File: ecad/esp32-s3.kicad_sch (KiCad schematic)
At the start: 1 part, among them U4 ESP32-S3

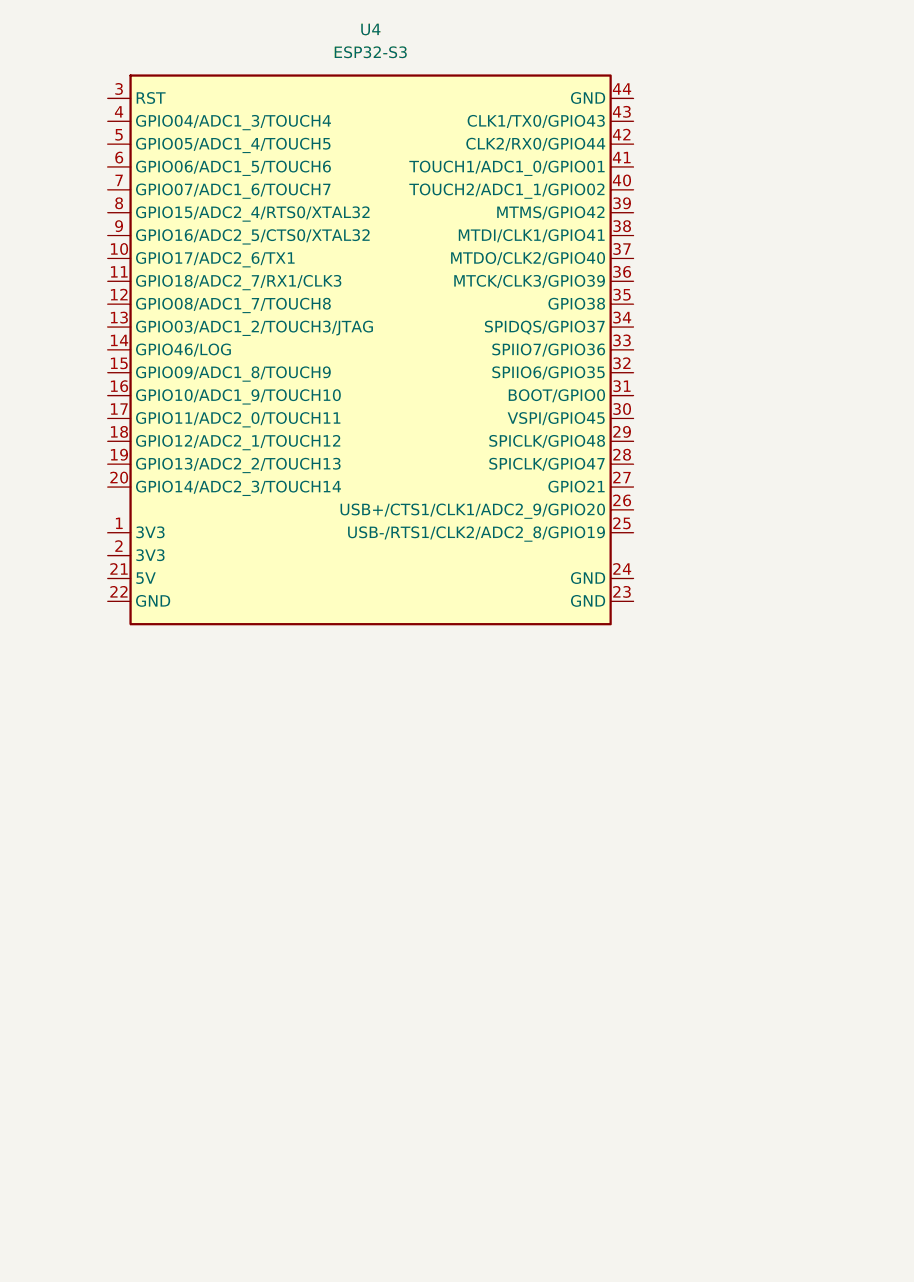
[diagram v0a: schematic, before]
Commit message: fead (ecad): update ESP32-S3 Schematic
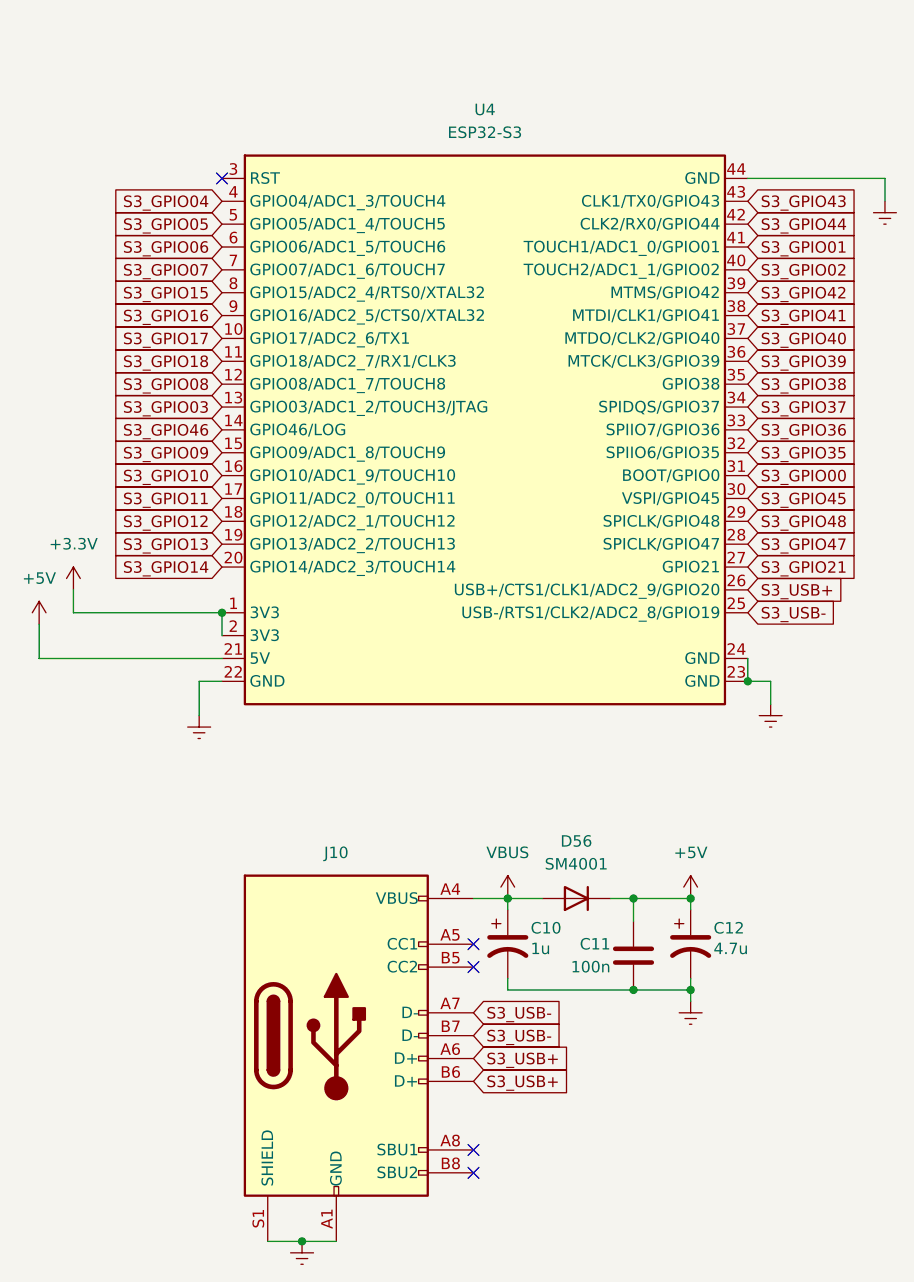
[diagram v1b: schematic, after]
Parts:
- added C10: 1u, Capacitor_SMD:CP_Elec_4x5.4, symbol Device:C_Polarized_US
- added C11: 100n, Capacitor_SMD:C_0805_2012Metric_Pad1.18x1.45mm_HandSolder, symbol Device:C
- added C12: 4.7u, Capacitor_SMD:CP_Elec_4x5.4, symbol Device:C_Polarized_US
- added D56: SM4001, Diode_SMD:D_MELF, symbol Diode:SM4001
- added J10: USB_C, Connector_USB:USB_C_Receptacle_Palconn_UTC16-G, symbol Connector:USB_C_Receptacle_USB2.0_16P
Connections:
- net +3.3V: now reaches U4.1 (3V3)
- net +3.3V: now also U4.2 (3V3)
- net S3_GPIO17: now reaches U4.10 (GPIO17/ADC2_6/TX1)
- net S3_GPIO18: now reaches U4.11 (GPIO18/ADC2_7/RX1/CLK3)
- net S3_GPIO08: now reaches U4.12 (GPIO08/ADC1_7/TOUCH8)
- net S3_GPIO03: now reaches U4.13 (GPIO03/ADC1_2/TOUCH3/JTAG)
- net S3_GPIO46: now reaches U4.14 (GPIO46/LOG)
- net S3_GPIO09: now reaches U4.15 (GPIO09/ADC1_8/TOUCH9)
- net S3_GPIO10: now reaches U4.16 (GPIO10/ADC1_9/TOUCH10)
- net S3_GPIO11: now reaches U4.17 (GPIO11/ADC2_0/TOUCH11)
- net S3_GPIO12: now reaches U4.18 (GPIO12/ADC2_1/TOUCH12)
- net S3_GPIO13: now reaches U4.19 (GPIO13/ADC2_2/TOUCH13)
- net S3_GPIO14: now reaches U4.20 (GPIO14/ADC2_3/TOUCH14)
- net +5V: now reaches U4.21 (5V)
- net +5V: now also C11.1, C12.1, D56.1 (K)
- net Earth: now reaches U4.22 (GND)
- net Earth: now also U4.23 (GND), U4.24 (GND), U4.44 (GND), C10.2, C11.2, C12.2, J10.A1 (GND), J10.A12 (GND), J10.B1 (GND), J10.B12 (GND), J10.S1 (SHIELD)
- net S3_USB-: now reaches U4.25 (USB-/RTS1/CLK2/ADC2_8/GPIO19)
- net S3_USB-: now also J10.A7 (D-), J10.B7 (D-)
- net S3_USB+: now reaches U4.26 (USB+/CTS1/CLK1/ADC2_9/GPIO20)
- net S3_USB+: now also J10.A6 (D+), J10.B6 (D+)
- net S3_GPIO21: now reaches U4.27 (GPIO21)
- net S3_GPIO47: now reaches U4.28 (SPICLK/GPIO47)
- net S3_GPIO48: now reaches U4.29 (SPICLK/GPIO48)
- net S3_GPIO45: now reaches U4.30 (VSPI/GPIO45)
- net S3_GPIO00: now reaches U4.31 (BOOT/GPIO0)
- net S3_GPIO35: now reaches U4.32 (SPIIO6/GPIO35)
- net S3_GPIO36: now reaches U4.33 (SPIIO7/GPIO36)
- net S3_GPIO37: now reaches U4.34 (SPIDQS/GPIO37)
- net S3_GPIO38: now reaches U4.35 (GPIO38)
- net S3_GPIO39: now reaches U4.36 (MTCK/CLK3/GPIO39)
- net S3_GPIO40: now reaches U4.37 (MTDO/CLK2/GPIO40)
- net S3_GPIO41: now reaches U4.38 (MTDI/CLK1/GPIO41)
- net S3_GPIO42: now reaches U4.39 (MTMS/GPIO42)
- net S3_GPIO04: now reaches U4.4 (GPIO04/ADC1_3/TOUCH4)
- net S3_GPIO02: now reaches U4.40 (TOUCH2/ADC1_1/GPIO02)
- net S3_GPIO01: now reaches U4.41 (TOUCH1/ADC1_0/GPIO01)
- net S3_GPIO44: now reaches U4.42 (CLK2/RX0/GPIO44)
- net S3_GPIO43: now reaches U4.43 (CLK1/TX0/GPIO43)
- net S3_GPIO05: now reaches U4.5 (GPIO05/ADC1_4/TOUCH5)
- net S3_GPIO06: now reaches U4.6 (GPIO06/ADC1_5/TOUCH6)
- net S3_GPIO07: now reaches U4.7 (GPIO07/ADC1_6/TOUCH7)
- net S3_GPIO15: now reaches U4.8 (GPIO15/ADC2_4/RTS0/XTAL32)
- net S3_GPIO16: now reaches U4.9 (GPIO16/ADC2_5/CTS0/XTAL32)
- new net VBUS: C10.1, D56.2 (A), J10.A4 (VBUS), J10.A9 (VBUS), J10.B4 (VBUS), J10.B9 (VBUS)
- no-connect marks 0 -> 5
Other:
- title: (none) -> ESP32 AK Shield Schematik drawing S3
- moved on the sheet: U4

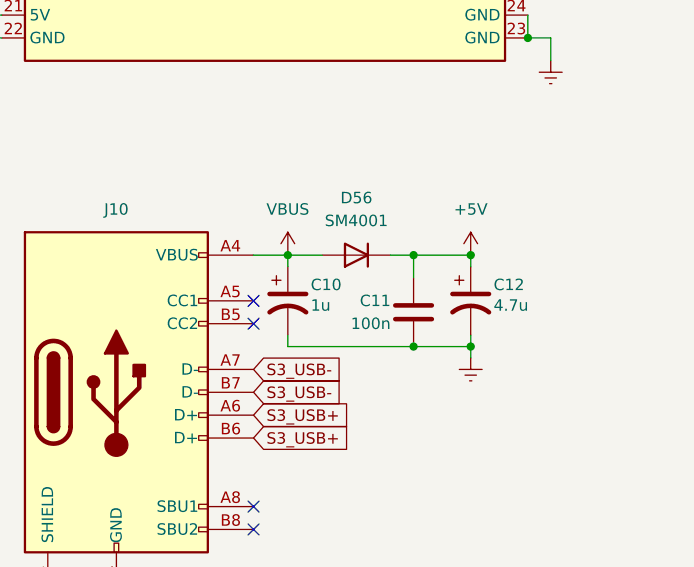
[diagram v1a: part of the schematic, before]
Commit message: feat (ecad): update PCB design
header pins and LEDs connected to devkits without ground-voltage
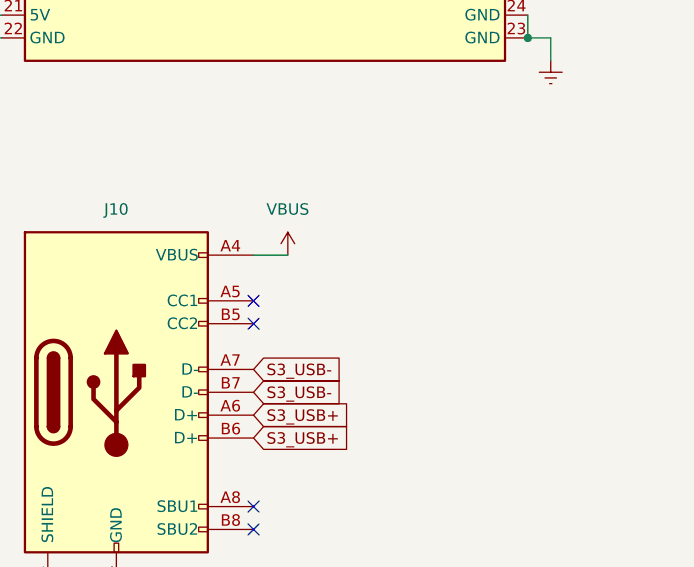
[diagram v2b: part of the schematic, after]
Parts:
- removed C10: 1u, Capacitor_SMD:CP_Elec_4x5.4, symbol Device:C_Polarized_US
- removed C11: 100n, Capacitor_SMD:C_0805_2012Metric_Pad1.18x1.45mm_HandSolder, symbol Device:C
- removed C12: 4.7u, Capacitor_SMD:CP_Elec_4x5.4, symbol Device:C_Polarized_US
- removed D56: SM4001, Diode_SMD:D_MELF, symbol Diode:SM4001
